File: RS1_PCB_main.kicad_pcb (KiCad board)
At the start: 2 copper layers, 47.5 x 39.5 mm, 49 parts, among them J1 Conn_01x05, J3 Connector, USB-TYPE-C-16P, J5 Conn_01x02, J7 Conn_01x02, J8 Conn_01x02, Q4 2N7002, SW3 GT-TC172A-H035-L1 (PWR BTN), U1 ESP32-C6-WROOM-1, U17 ME6217C33M5G, U2 USBLC6-2SC6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

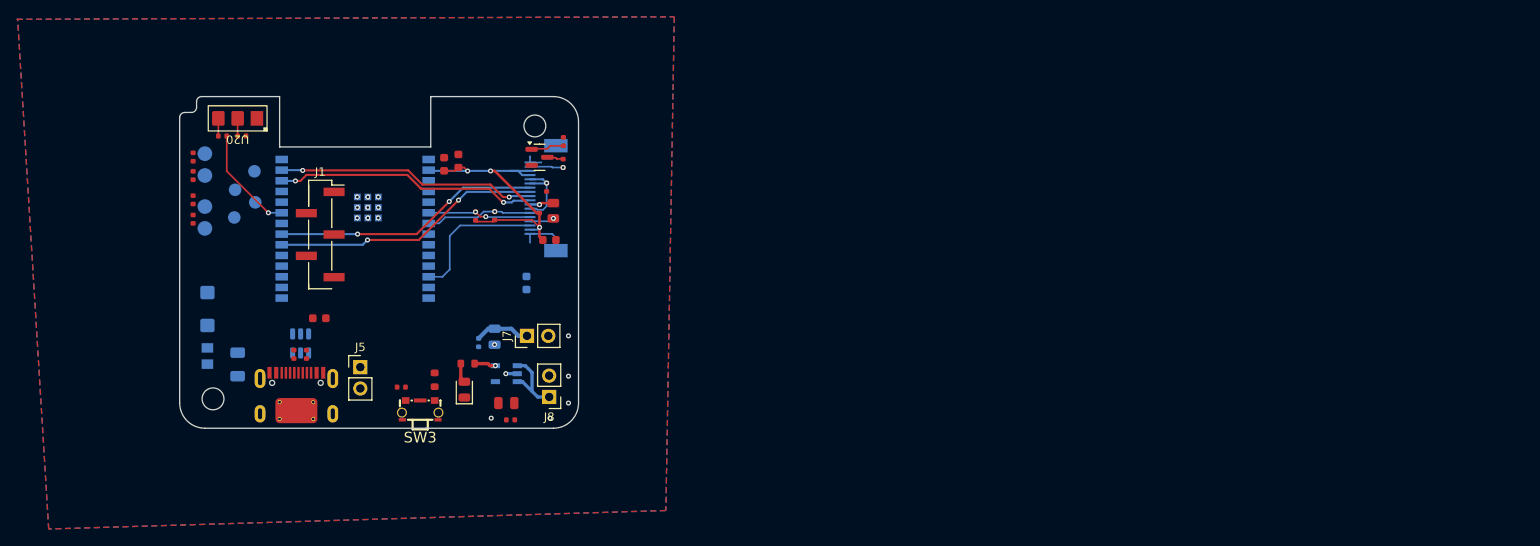
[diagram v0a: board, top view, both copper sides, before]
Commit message: changed layout
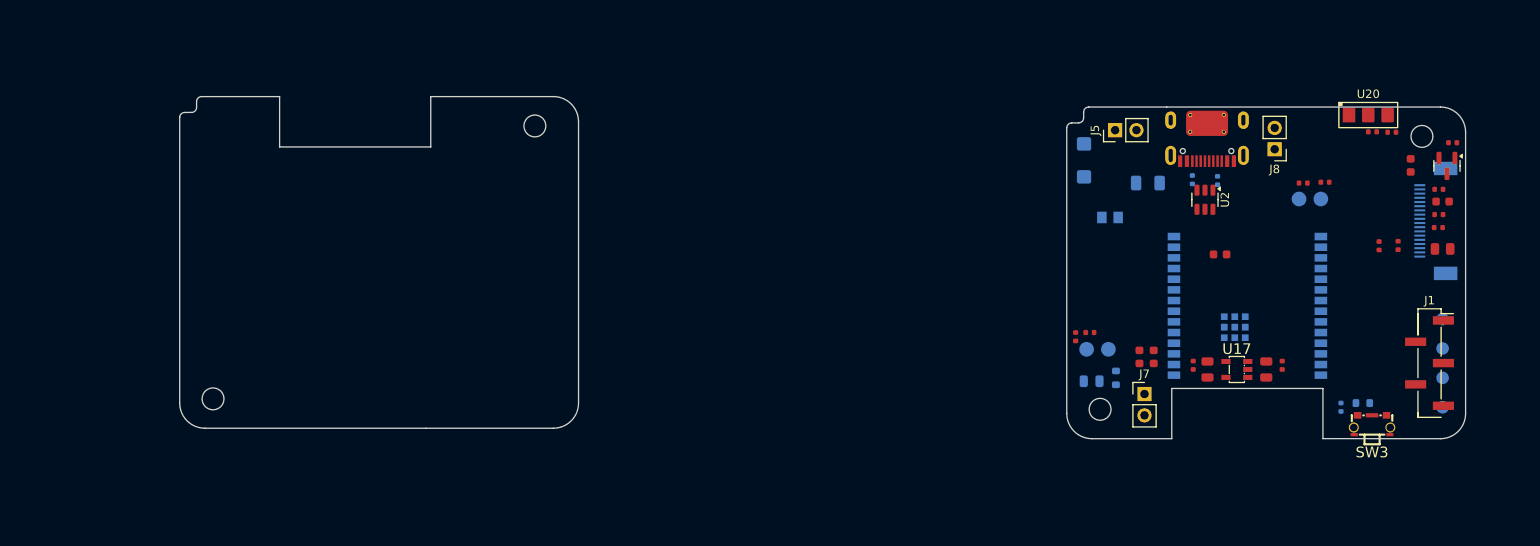
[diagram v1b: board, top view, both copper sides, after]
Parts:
- C15, C25, C5, U17, U2: moved to F.Cu
- C6, D3, R1, R2, R21, R5: moved to B.Cu
- moved TP3 145.5 mm to (191.5, 74.0)
- moved TP6 144.7 mm to (191.5, 70.5)
- moved TP4 143.5 mm to (191.5, 77.5)
- moved TP5 142.6 mm to (191.5, 67.0)
- moved R12 139.3 mm to (185.4, 44.8)
- moved R9 134.8 mm to (177.5, 50.7), turned to 180 degrees
- moved R29 134.7 mm to (183.2, 44.7)
- moved U20 134.7 mm to (182.7, 42.7), turned to 0 degrees
- moved J1 133.0 mm to (189.9, 72.2)
- moved C3 132.3 mm to (174.9, 50.8), turned to 180 degrees
- moved U7 131.6 mm to (175.7, 52.7), turned to 180 degrees
- moved SW3 113.4 mm to (183.1, 79.6)
- moved J3 112.6 mm to (163.4, 45.7), turned to 180 degrees
- moved C6 111.9 mm to (179.4, 77.5), turned to -90 degrees
- moved R1 111.9 mm to (164.7, 50.5)
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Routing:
- net +3.3V: track 47.7 -> 0.51 mm, vias 4 -> 0
- net /LCD_CS: track 32.2 -> 0.00 mm, vias 2 -> 0
- net /LCD_DC: track 31.9 -> 0.00 mm, vias 2 -> 0
- net /LCD_MOSI: track 31.2 -> 0.00 mm, vias 2 -> 0
- net /LCD_SCLK: track 31.0 -> 0.00 mm, vias 2 -> 0
- net GND: track 18.4 -> 0.00 mm, vias 17 -> 0
- net /TP_INT: track 17.0 -> 0.00 mm
- net /Enc_B: track 12.8 -> 0.00 mm, vias 1 -> 0
- net /SCL: track 12.7 -> 0.00 mm, vias 1 -> 0
- net /SDA: track 12.4 -> 0.01 mm, vias 2 -> 0
- net /VSYS: track 8.89 -> 0.00 mm
- net /LED_K: track 3.98 -> 0.00 mm, vias 1 -> 0
- net /LCD_BL: track 3.96 -> 0.00 mm
- net /LCD_RST: track 3.12 -> 0.00 mm, vias 1 -> 0
- net /TP_RST: track 2.92 -> 0.00 mm, vias 1 -> 0
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- removed copper zone on B.Cu, net GND
- removed copper zone on F.Cu, net GND
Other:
- board size 47.5 x 39.5 mm -> 153.1 x 40.7 mm

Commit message: changed layout (position ldo, pins...)
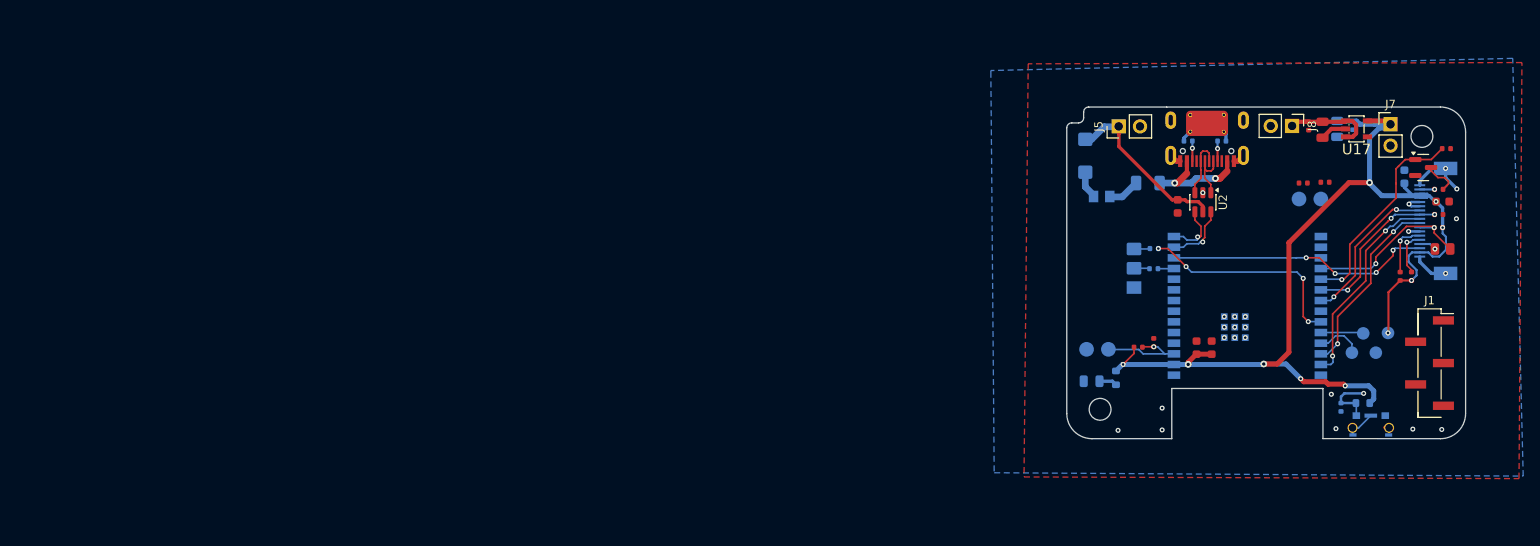
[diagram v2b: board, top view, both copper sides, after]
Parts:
- C15, C25, C5, R12, R29, SW3, U20: moved to B.Cu
- moved J7 43.5 mm to (185.3, 43.8)
- moved C25 34.3 mm to (180.8, 44.0)
- moved U20 33.3 mm to (154.8, 61.0), turned to 90 degrees
- moved C5 32.6 mm to (178.9, 44.4)
- moved U17 32.0 mm to (181.2, 44.4), turned to 180 degrees
- moved R12 31.5 mm to (157.2, 58.6)
- moved R29 30.7 mm to (157.1, 61.0)
- moved C2 29.3 mm to (177.2, 44.5)
- moved C23 28.7 mm to (175.6, 44.0)
- moved TP4 12.9 mm to (182.1, 68.7)
- moved TP3 11.2 mm to (180.7, 71.0)
- moved TP5 8.90 mm to (183.6, 71.0)
- moved C4 7.69 mm to (157.1, 69.8), turned to 90 degrees
- moved C1 7.63 mm to (159.9, 53.6), turned to -90 degrees
- moved R13 7.55 mm to (155.2, 70.3), turned to 0 degrees
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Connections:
- U2 pad 1: /D+ -> /D-
- U2 pad 3: /D- -> /D+
- U2 pad 4: /USB_N -> /USB_P
- U2 pad 6: /USB_P -> /USB_N
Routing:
- net +3.3V: track 0.51 -> 124.0 mm, vias 0 -> 10
- net /TP_INT: track 0.00 -> 31.7 mm, vias 0 -> 4
- net /Enc_B: track 0.00 -> 25.6 mm, vias 0 -> 4
- net /LCD_BL: track 0.00 -> 25.0 mm, vias 0 -> 1
- net /LCD_SCLK: track 0.00 -> 24.5 mm, vias 0 -> 2
- net GND: track 0.00 -> 24.2 mm, vias 0 -> 23
- net /LCD_MOSI: track 0.00 -> 22.2 mm, vias 0 -> 2
- net /LCD_RST: track 0.00 -> 21.2 mm, vias 0 -> 2
- net +5V: track 0.00 -> 20.6 mm
- net /LCD_CS: track 0.00 -> 19.3 mm, vias 0 -> 3
- net /LCD_DC: track 0.00 -> 18.3 mm, vias 0 -> 2
- net Net-(F1-Pad1): track 0.00 -> 13.2 mm, vias 0 -> 2
- net /EN: track 0.00 -> 11.0 mm, vias 0 -> 1
- net /VSYS: track 0.00 -> 11.0 mm
- net /D-: track 0.00 -> 8.03 mm
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- added copper zone on B.Cu, net GND
- added copper zone on F.Cu, net GND
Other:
- board size 153.1 x 40.7 mm -> 47.5 x 39.5 mm

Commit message: all connected
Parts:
- C3, R9: moved to B.Cu
- moved J1 25.3 mm to (168.2, 59.4)
- moved TP3 11.5 mm to (191.8, 74.0)
- moved TP5 10.2 mm to (191.8, 65.0)
- moved TP4 9.97 mm to (191.8, 71.0)
- moved TP6 6.78 mm to (191.8, 68.0)
- moved C25 4.14 mm to (176.7, 43.8)
- moved R9 3.26 mm to (175.1, 48.5)
- moved C3 3.05 mm to (172.9, 48.5)
- moved U7 2.97 mm to (173.7, 50.5)
- moved C23 2.69 mm to (174.6, 46.5), turned to 180 degrees
- moved R23 0.50 mm to (191.6, 54.5)
- moved C6 0.43 mm to (179.7, 77.2)
- moved SW3 0.41 mm to (182.9, 79.2)
- moved R2 0.34 mm to (182.0, 76.7)
- moved J8 0.33 mm to (173.2, 44.0)
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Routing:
- net /SDA: track 5.43 -> 43.9 mm, vias 1 -> 3
- net /SCL: track 6.38 -> 44.7 mm, vias 1 -> 3
- net /PWR-KEY: track 7.03 -> 31.5 mm, vias 1 -> 2
- net +3.3V: track 124.0 -> 140.7 mm
- net /BOOT: track 0.00 -> 14.5 mm, vias 0 -> 2
- net /INT_B: track 0.00 -> 13.6 mm, vias 0 -> 1
- net Net-(U1-U0TXD/GPIO16): track 5.51 -> 17.2 mm
- net /PWM_LED: track 0.00 -> 11.3 mm, vias 0 -> 1
- net Net-(U1-U0RXD/GPIO17): track 5.09 -> 15.7 mm
- net /SERVO_PWM: track 0.00 -> 7.69 mm, vias 0 -> 1
- net GND: track 24.2 -> 29.8 mm, vias 23 -> 25
- net /VSYS: track 11.0 -> 14.6 mm
- net unconnected-(SW3-Pad4): track 0.72 -> 1.60 mm
- net /LCD_CS: track 19.3 -> 19.8 mm
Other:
- outline, holes or cut-outs redrawn

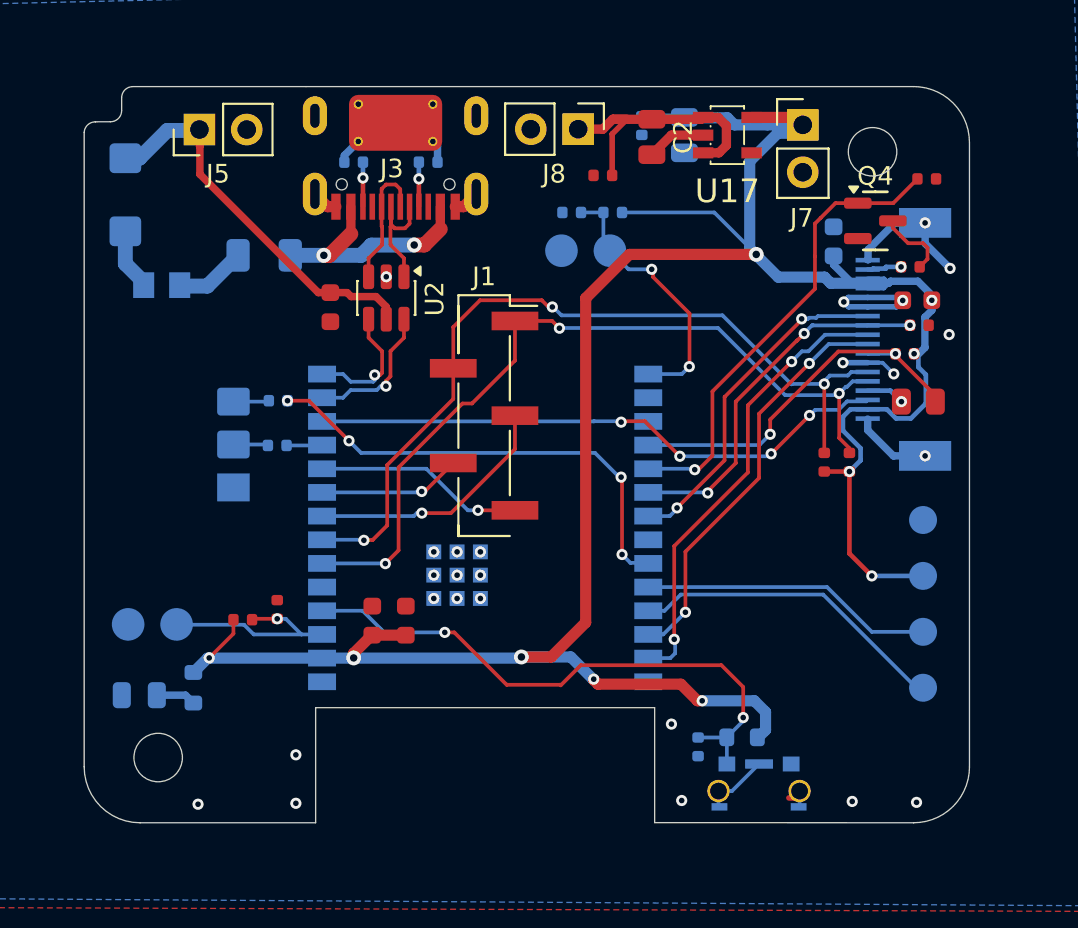
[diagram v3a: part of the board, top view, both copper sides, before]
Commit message: changed testpoints, worked on silkprints
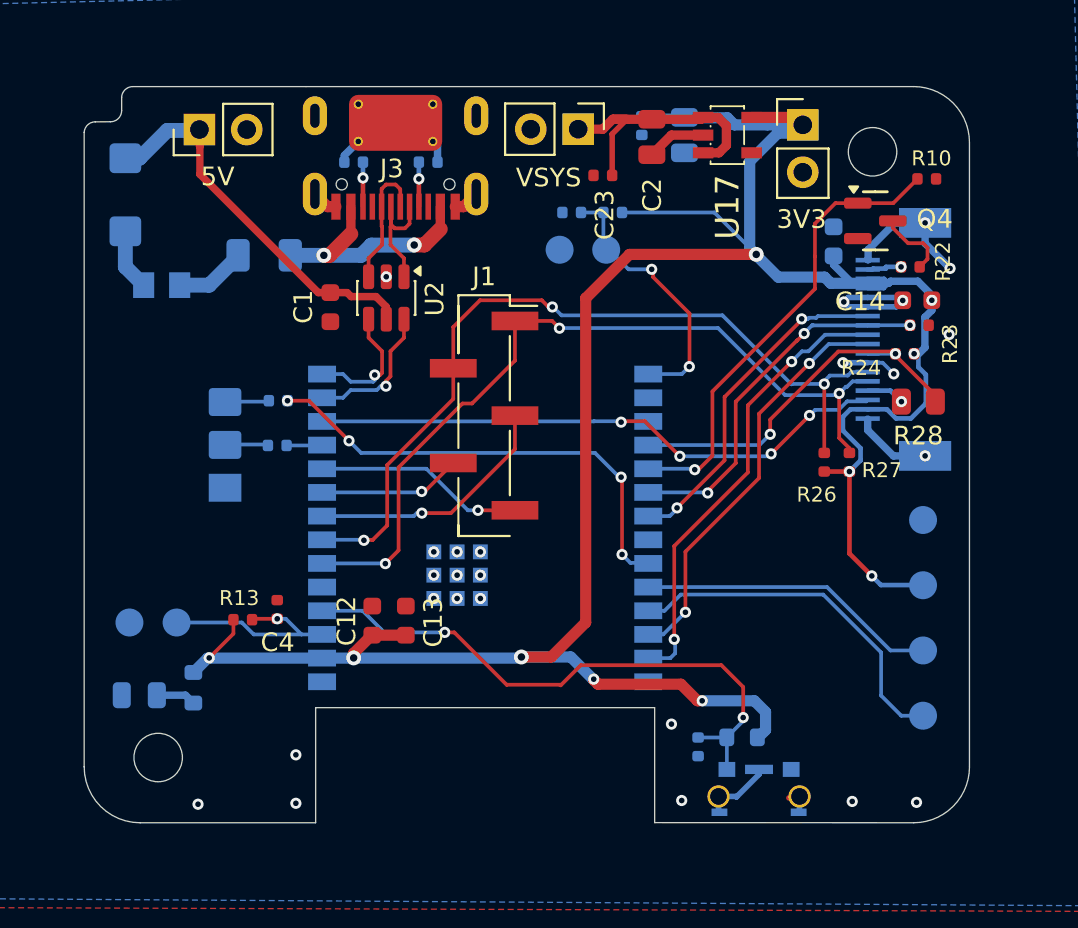
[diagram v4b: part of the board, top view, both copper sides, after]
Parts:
- removed U7: BOOT, ESP32_C6_libfoot:TP_1.75mm_2Points
- removed U8: RST, ESP32_C6_libfoot:TP_1.75mm_2Points
- added TP1: BOOT, TestPoint:TestPoint_Pad_D1.5mm, B.Cu at (174.8, 50.5)
- added TP2: -, TestPoint:TestPoint_Pad_D1.5mm, B.Cu at (172.2, 50.5)
- added TP7: RST, TestPoint:TestPoint_Pad_D1.5mm, B.Cu at (151.7, 70.5)
- added TP8: -, TestPoint:TestPoint_Pad_D1.5mm, B.Cu at (149.2, 70.5)
- moved TP3 1.50 mm to (191.8, 75.5)
- moved TP4 1.00 mm to (191.8, 72.0)
- moved TP6 0.50 mm to (191.8, 68.5)
- moved U20 0.45 mm to (154.3, 61.0)
- moved SW3 0.29 mm to (182.9, 79.5)
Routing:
- net Net-(U1-U0TXD/GPIO16): track 17.2 -> 19.2 mm
- net unconnected-(SW3-Pad3): track 3.65 -> 4.68 mm
- net unconnected-(SW3-Pad4): track 1.60 -> 2.40 mm
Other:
- board text added: "3V3"
- board text added: "5V"
- board text added: "VSYS"

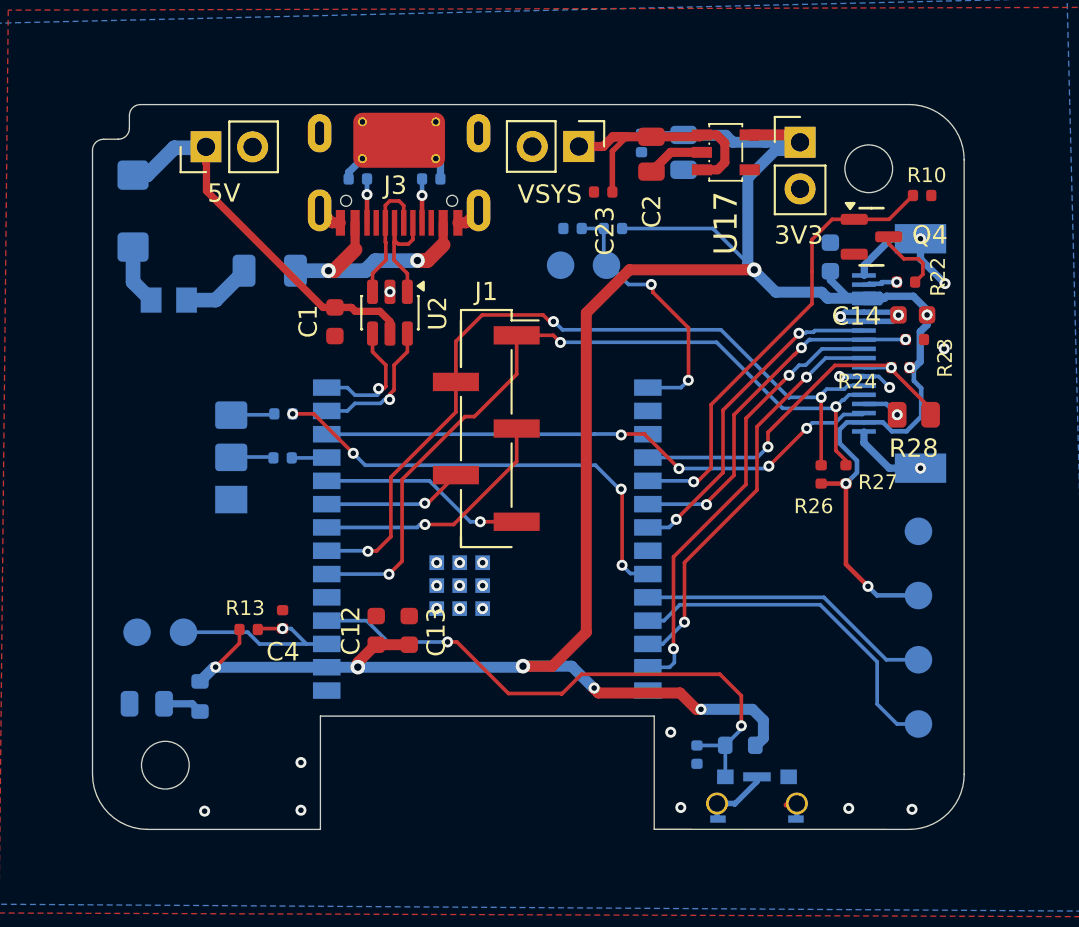
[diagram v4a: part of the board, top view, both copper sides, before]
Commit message: fixed hole position and touchingpoints of housing
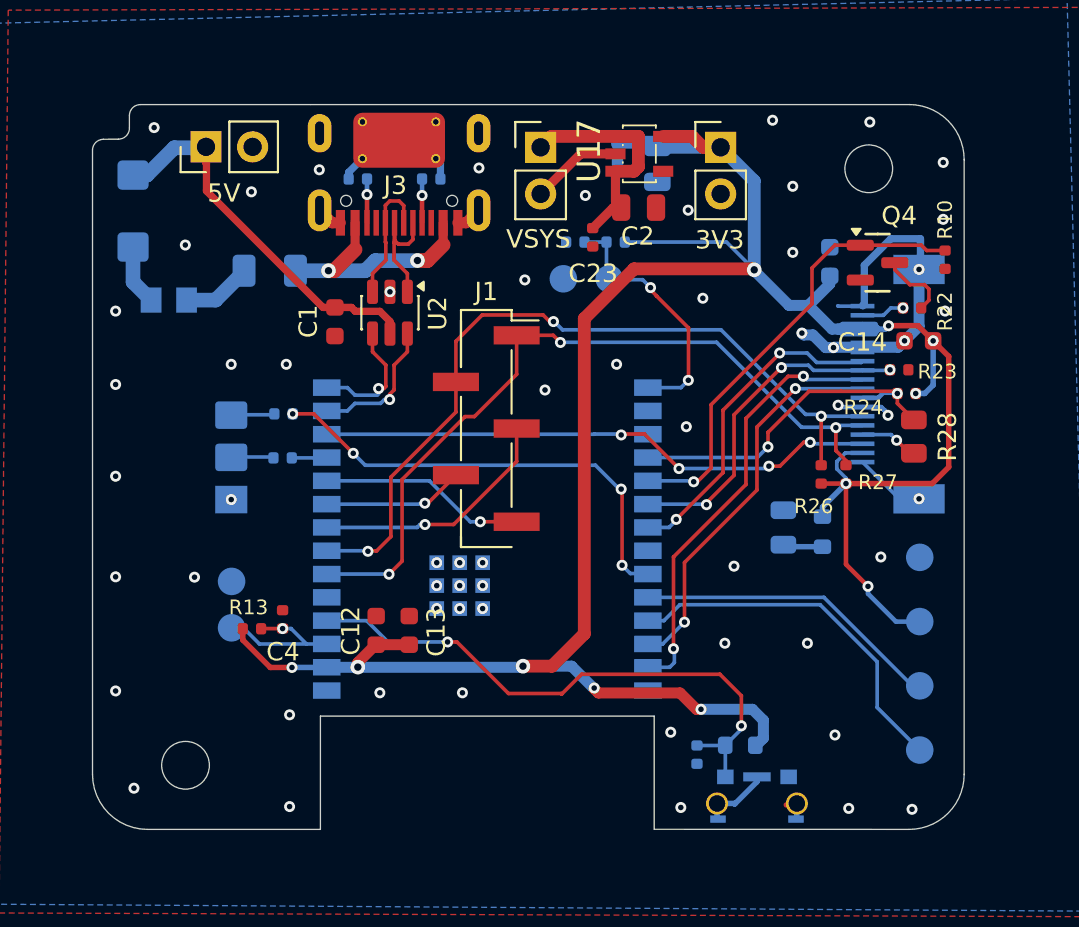
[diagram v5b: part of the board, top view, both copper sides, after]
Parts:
- moved D3 36.0 mm to (184.4, 64.8), turned to -90 degrees
- moved R5 35.1 mm to (186.5, 65.0)
- moved TP8 5.85 mm to (154.3, 67.7), turned to 90 degrees
- moved U17 4.71 mm to (176.5, 44.4)
- moved J7 4.34 mm to (181.0, 44.1)
- moved R10 3.72 mm to (193.2, 50.2), turned to 90 degrees
- moved C2 2.99 mm to (176.5, 47.4), turned to 0 degrees
- moved TP7 2.63 mm to (154.3, 70.3), turned to 90 degrees
- moved C23 2.53 mm to (174.0, 49.0), turned to -90 degrees
- moved J8 2.09 mm to (171.2, 44.1), turned to 0 degrees
- moved R23 1.86 mm to (190.7, 56.2)
- moved FPC2 1.67 mm to (190.2, 57.0)
- moved C5 1.57 mm to (177.5, 45.0)
- moved R24 1.45 mm to (191.1, 57.5)
- moved C14 1.45 mm to (191.8, 54.6)
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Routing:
- net GND: track 29.8 -> 36.3 mm, vias 25 -> 59
- net +3.3V: track 140.4 -> 145.6 mm, vias 10 -> 11
- net /EN: track 11.1 -> 8.37 mm
- net /VSYS: track 14.6 -> 12.7 mm
- net /LCD_RST: track 21.1 -> 19.6 mm
- net /LCD_CS: track 19.8 -> 18.5 mm
- net /TP_RST: track 2.05 -> 3.23 mm
- net /SCL: track 44.7 -> 43.7 mm
- net /SDA: track 43.9 -> 42.9 mm
- net /LCD_MOSI: track 22.2 -> 21.4 mm
- net Net-(U1-U0TXD/GPIO16): track 19.2 -> 19.9 mm
- net /TP_INT: track 31.4 -> 30.6 mm
- net Net-(U1-U0RXD/GPIO17): track 16.2 -> 16.8 mm
- net /LCD_SCLK: track 24.5 -> 23.9 mm
- net /BOOT: track 14.5 -> 13.9 mm
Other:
- outline, holes or cut-outs redrawn
